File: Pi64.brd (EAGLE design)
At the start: 130.7 x 72.9 mm, 117 parts, among them J1 USB-MINIB-5PIN, J2 AVR_SPI, J3 FTDI_DEVICERA_SMT, J4 FTDI_DEVICERA_SMT, SW1 LEFT, SW2 RIGHT, SW3 PWR_SWITCH, SW8 OS102011MA1Q, U1 MIC7221, U2 MCP1642B-ADJ, U3 PAM2306AYPKE, U4 LM4875, U5 Mic5365-2.8Y, U7 AZV321, X2 HEADPHONE

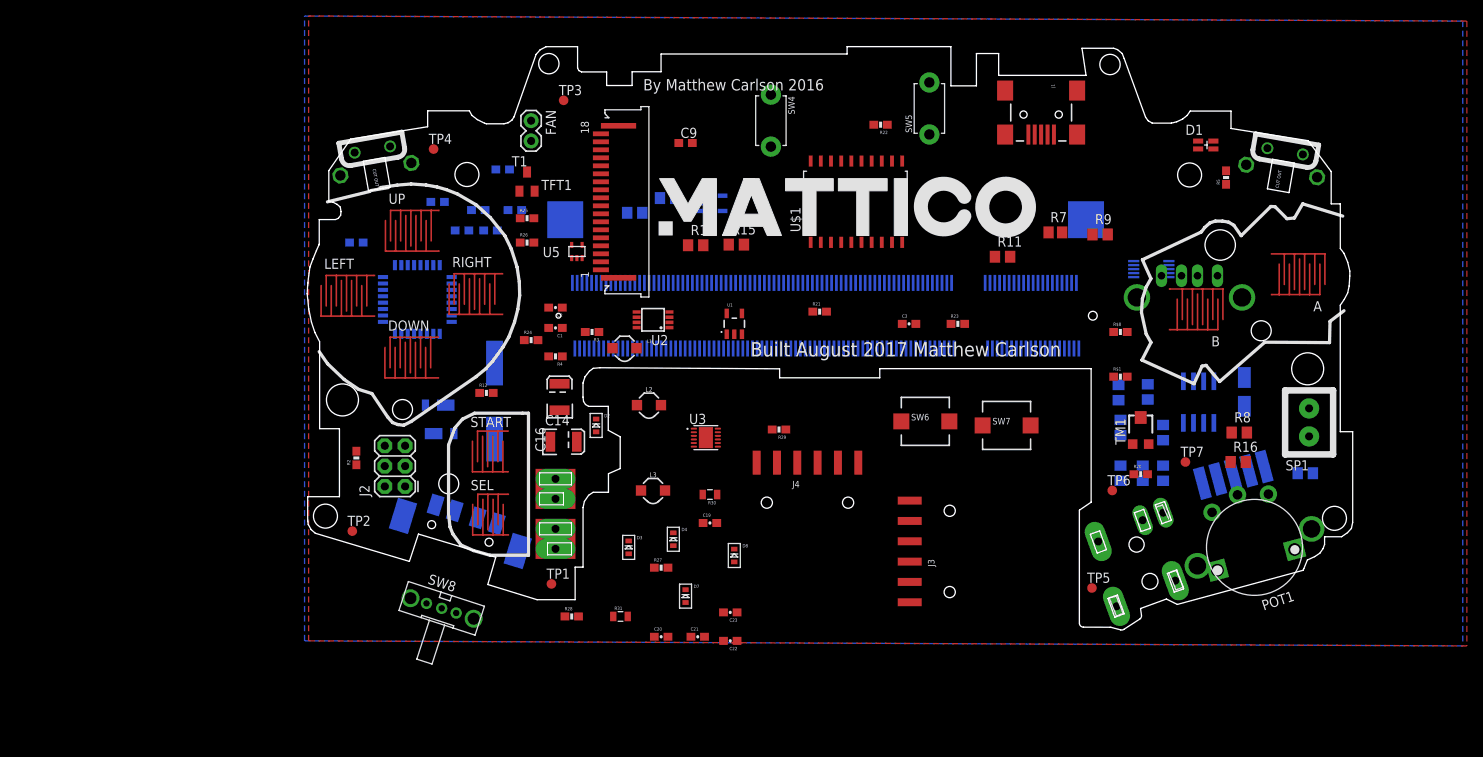
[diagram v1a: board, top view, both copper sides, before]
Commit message: Removed old stuff and started new circuit board design
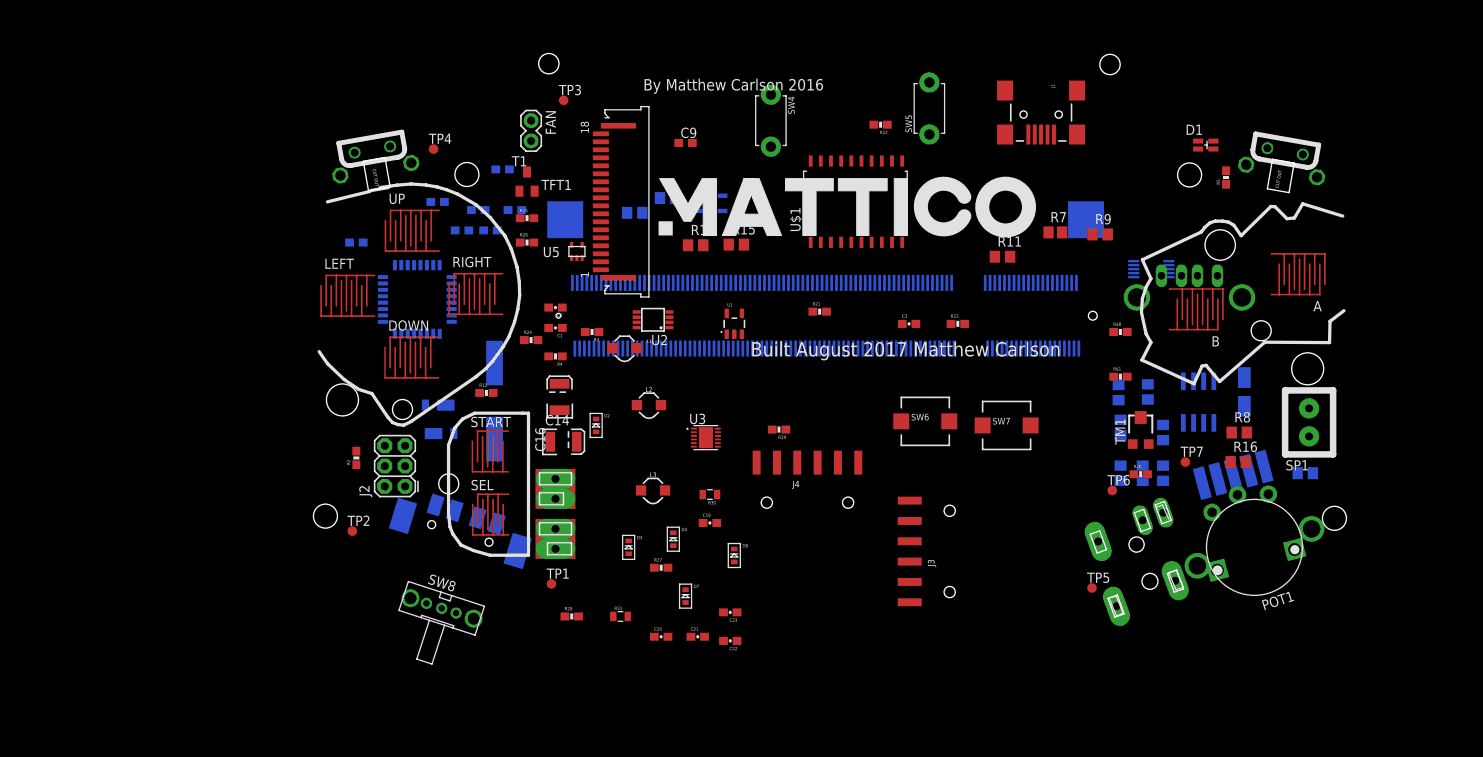
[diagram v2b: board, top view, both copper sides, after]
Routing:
- removed copper zone on layer 1, net GND
- removed copper zone on layer 16, net GND
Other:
- board size 130.7 x 72.9 mm -> 11.7 x 14.5 mm

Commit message: removed a lot of cruft and added STM32F
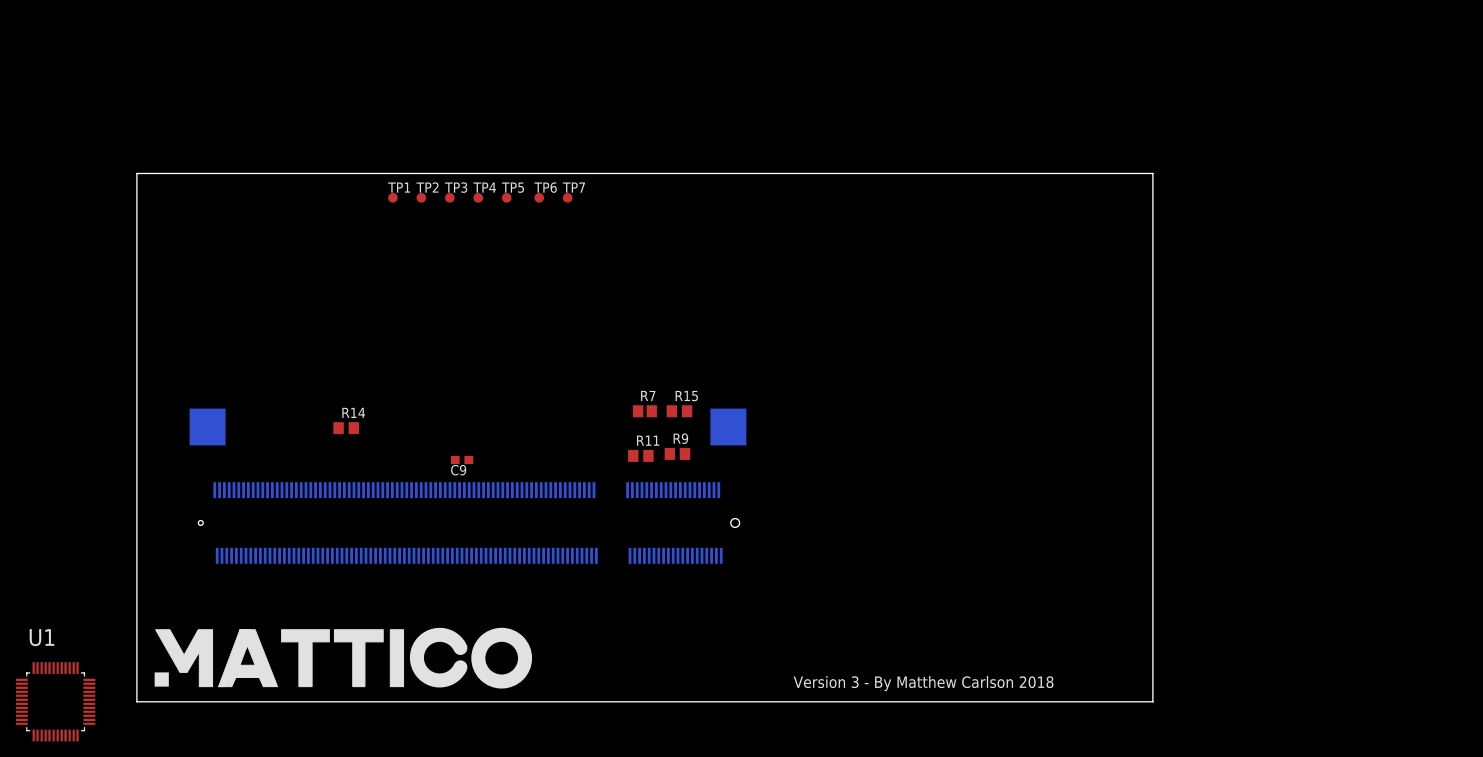
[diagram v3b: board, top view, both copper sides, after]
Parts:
- removed A, B, DOWN, LEFT, RIGHT, UP: GBA_BTN_CONDUCTIVE, GBA:GBA_BUTTON_CONDUCTIVE
- removed BT1: (no value), custom:GBA_BATTERY
- removed C1, C19, C2, C3: 100nF, SparkFun-Capacitors:0603-CAP
- removed C10: 1.0uF, SparkFun-Capacitors:0603-CAP
- removed C11, C12: 22pF, SparkFun-Capacitors:0603-CAP
- removed C13, C15, C18, C5, C6: 10u, rcl:C0805
- removed C14, C16: 47uF, SparkFun-Capacitors:EIA3528
- removed C17: 100n, rcl:C0805
- removed C20, C21, C22, C23: 10uF, SparkFun-Capacitors:0603-CAP
- removed C4: 220n, rcl:C0805
- removed C7: 100uF, rcl:153CLV-0405
- removed C8: 330n, rcl:C0805
- removed COPRO: MEGA16u2, adafruit:TQFP32-08
- removed D1: DUAL_LED, custom:DUAL_LED
- removed D2, D3, D4, D7, D8: (no value), adafruit:SOD-523
- removed D5, D6: (no value), custom:DIODE_POWERDI_123
- removed FAN: (no value), SparkFun-Connectors:1X02
- removed J1: USB-MINIB-5PIN, SparkFun-Connectors:USB-MINIB
- removed J2: AVR_SPI, SparkFun-Connectors:2X3
- removed J3, J4: FTDI_DEVICERA_SMT, SparkFun-Connectors:FTDI_DEVICE_RA_SMT
- removed L1: 4.7uH, SparkFun-Passives:INDUCTOR_4.7UH
- removed L2, L3: 4.7µH/±30%/1.2A, SparkFun-Coils:INDUCTOR_4.7UH
- removed POT1: THUMBPOT, adafruit:THUMBWHEEL
- removed R$1: 976kR, SparkFun-Resistors:0603-RES
- removed R$8: 430kR, SparkFun-Resistors:0603-RES
- removed R1: 27k, GBA:VOLUME
- removed R10: 3R9, rcl:R0805
- removed R12: 1K, SparkFun-Resistors:0603-RES
- removed R13, R2, R21, R22, R25, R26: 4.7K, SparkFun-Resistors:0603-RES
- removed R16, R8: 270R, rcl:R0805
- removed R17, R18: 22, SparkFun-Resistors:0603-RES
- removed R19, R24, R27, R28: 10K, SparkFun-Resistors:0603-RES
- removed R20, R5: 680, SparkFun-Resistors:0603-RES
- removed R23, R29, R3: 100k, SparkFun-Resistors:0603-RES
- removed R30, R31: (no value), SparkFun-Resistors:0805
- removed R4: 270, SparkFun-Resistors:0603-RES
- removed R6: 100k, rcl:R0805
- removed SEL, START: BUTTON-CONDUCTIVESMD, SparkFun-Electromechanical:BUTTON-CONDUCTIVE
- removed SP1: SPEAKER, GBA:SPEAKER
- removed SW1: LEFT, GBA:BUMPER
- removed SW2: RIGHT, GBA:BUMPER
- removed SW3: PWR_SWITCH, GBA:PWR_SWITCH
- removed SW4, SW5: (no value), adafruit:TACT_PANA-EVQ
- removed SW6, SW7: (no value), adafruit:PUSHBUTTON_SMD_SJ
- removed SW8: OS102011MA1Q, adafruit:OS102011MA1Q
- removed T1: (no value), custom:TRANSISTOR_SC59-BEC
- removed TFT1: GBA_TFT, GBA:GBA_TFT
- removed TM1: (no value), adafruit:TC33X
- removed U$1: CBT3244AD, custom:S020-75MM
- removed U$3: MCP48FEB01-E/UN, custom:10-MSOP
- removed U$5: CRYSTAL-ABLS, custom:HC49/US
- removed U2: MCP1642B-ADJ, custom:MICROCHIP_MSOP8
- removed U3: PAM2306AYPKE, custom:SON45P300X300X80-13N
- removed U4: LM4875, texas:SOIC8
- removed U5: Mic5365-2.8Y, SparkFun-PowerIC:SC70
- removed U7: AZV321, GBA:SOT23-5
- removed X1: (no value), Adafruit_PowerBoost:MICROBUILDER_USB_HOST-PTH
- removed X2: HEADPHONE, GBA:HEADPHONE
- U1: value MIC7221 -> STM32F103CBT6; device custom:SPARKFUN-ANALOGIC_SOT23-5 -> custom:QFP50P900X900X160-48N
- moved U1 97.1 mm to (-10.2, 0.00)
- moved TP5 87.9 mm to (46.2, 63.0)
- moved U$2 84.5 mm to (1.58, 1.14)
- moved TP7 84.0 mm to (53.8, 63.0)
- moved TP6 80.4 mm to (50.3, 63.0)
- moved R9 59.5 mm to (67.6, 31.0)
- moved R7 56.0 mm to (63.5, 36.3)
- moved TP1 52.2 mm to (32.0, 63.0)
- moved PCB1 51.7 mm to (41.7, 22.4)
- moved R11 51.6 mm to (63.0, 30.7)
- moved R14 49.3 mm to (26.2, 34.2)
- moved C9 48.5 mm to (40.6, 30.2), turned to 180 degrees
- moved TP2 42.5 mm to (35.6, 63.0)
- moved FRAME2 29.0 mm to (32.0, -9.65)
- moved R15 22.0 mm to (67.8, 36.3)
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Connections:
- removed net BATT_LOW: D1.1, D1.3, D8.A, R3.2, U1.1
- removed net COPRO_D+: R18.1
- removed net COPRO_D-: R17.1
- removed net COPRO_DC: COPRO.20, U$1.P$8
- removed net COPRO_MISO: COPRO.17, J2.1, U$3.8
- removed net COPRO_MOSI: COPRO.16, J2.4, U$1.P$4, U$3.10
- removed net COPRO_RESET: COPRO.24, J2.5, R19.1
- removed net COPRO_RX: COPRO.8
- removed net COPRO_SCK: COPRO.15, J2.3, U$1.P$2, U$3.9
- removed net COPRO_TFT_RESET: COPRO.14, U$1.P$6
- removed net COPRO_TX: COPRO.9
- removed net DAC_CS: COPRO.19, U$3.2
- removed net DAC_OUT: R16.1, U$3.4
- removed net DAC_REF: U$3.3
- removed net EXP: U3.13
- removed net FAN_EN: R12.2
- removed net N$10: R22.1, U$1.P$19
- removed net N$11: C5.1, U4.7
- removed net N$12: COPRO.5, R28.1
- removed net N$13: C7.-, X2.L, X2.R
- removed net N$14: C7.+, SP1.1, U4.5
- removed net N$15: SP1.2, U4.8
- removed net N$16: R6.1, U4.3, X2.2
- removed net N$18: R21.1, U$1.P$1
- removed net N$19: COPRO.30, R17.2
- removed net N$2: C4.1, C8.1, R16.2, R8.2
- removed net N$21: R10.2, TFT1.10
- removed net N$22: COPRO.29, R18.2
- removed net N$23: R$1.1, R$8.2, U2.2
- removed net N$24: R10.1, U7.3, U7.4
- removed net N$25: C10.1, COPRO.27
- removed net N$28: C11.1, COPRO.1, U$5.P$2
- removed net N$29: C12.1, COPRO.2, U$5.P$1
- removed net N$3: D7.A, D8.K
- removed net N$31: D3.A, D4.K
- removed net N$32: L3.P$1, U3.2
- removed net N$33: D3.K, D7.K, R27.2, R28.2
- removed net N$34: L1.P$2, U2.5
- removed net N$38: COPRO.22, R27.1
- removed net N$39: FAN.1, T1.C
- removed net N$4: C2.1, R3.1, TM1.2, U1.3
- removed net N$40: R12.1, T1.B
- removed net N$44: COPRO.6, R24.1
- removed net N$45: C14.A, D5.2, D6.2, L1.P$1, SW8.2, U2.8
- removed net N$46: C19.1, R29.1, U3.12
- removed net N$47: L2.P$1, U3.8
- removed net N$49: R31.2, U3.4
- removed net N$5: C1.1, R4.1, U1.4
- removed net N$50: R30.1, U3.10
- removed net N$6: D1.4, R5.1
- removed net N$7: D1.2, R20.2
- removed net N$8: POT1.2, U4.4
- removed net N$9: C4.2, U4.2
- removed net PWR_DOWN: D2.A, D4.A, SW8.1
- removed net PWR_UP: D2.K, R23.2, R24.2, U2.1
- removed net TFT_CS: COPRO.10, TFT1.5
- removed net TFT_DC: TFT1.4, U$1.P$12, U$1.P$3
- removed net TFT_MOSI: TFT1.6, U$1.P$16, U$1.P$7
- removed net TFT_RESET: TFT1.2, U$1.P$14, U$1.P$5
- removed net TFT_SCLK: TFT1.3, U$1.P$18, U$1.P$9
- removed net USB_GND: J1.GND
- removed net V_BATT: BT1.BT+1, BT1.BT+2, D6.1, R4.2
- removed net V_USB: D5.1, J1.VBUS
- new net +3V3: U1.1, U1.24, U1.36, U1.48, U1.9
- new net PA11: U1.32
- net 1.8V: no longer C20.1, L3.P$2, R30.2
- net 2.8V: no longer C13.1, TFT1.9, U5.5
- net 3.3V: no longer C21.1, COPRO.31, COPRO.32, COPRO.4, L2.P$2, R13.2, R2.2, R21.2, R22.2, R25.2, R26.2, R31.1, U$1.P$20, U$3.1
- net 5V: no longer C15.1, C16.A, C17.1, C18.1, C22.1, C23.1, C3.1, C6.2, FAN.2, J2.2, POT1.3, R$1.2, R19.2, R29.2, R5.2, R6.2, TM1.3, U1.2, U2.4, U3.1, U3.6, U3.7, U4.1, U5.1, U5.3, U7.5, X1.VBUS
- net A_BTN: no longer A.2
- net B_BTN: no longer B.2
- net DOWN_BTN: no longer DOWN.2
- net GND: no longer A.1, B.1, BT1.BT-1, BT1.BT-2, C1.2, C10.2, C11.2, C12.2, C13.2, C14.C, C15.2, C16.C, C17.2, C18.2, C19.2, C2.2, C20.2, C21.2, C22.2, C23.2, C3.2, C5.2, C6.1, C8.2, COPRO.28, COPRO.3, DOWN.1, J2.6, J3.6, J4.6, LEFT.1, POT1.1, R$8.1, R20.1, R23.1, RIGHT.1, SEL.1, START.1, SW1.1, SW2.1, SW4.P$2, SW5.P$2, SW6.P$2, SW7.P$2, T1.E, TFT1.1, TFT1.11, TFT1.12, TFT1.13, TFT1.14, TFT1.8, TM1.1, U$1.P$10, U$3.7, U1.5, U2.6, U2.7, U3.3, U3.9, U4.6, U5.2, U7.2, UP.1, X1.GND, X2.1, X2.GND
- net L1_BTN: no longer SW1.2
- net L2_BTN: no longer R2.1, SW4.P$1
- net LEFT_BTN: no longer LEFT.2
- net PI_MOSI: no longer U$1.P$13
- net PI_PWM0: no longer R8.1
- net PI_SCK: no longer U$1.P$11
- net PI_TFT_DC: no longer U$1.P$17
- net PI_TFT_RESET: no longer U$1.P$15
- net R1_BTN: no longer SW2.2
- net R2_BTN: no longer R13.1, SW5.P$1
- net RIGHT_BTN: no longer RIGHT.2
- net SELECT_BTN: no longer SEL.2
- net START_BTN: no longer START.2
- net TFT_LED: no longer U7.1
- net UP_BTN: no longer UP.2
- net X_BTN: no longer R26.1, SW6.P$1
- net Y_BTN: no longer R25.1, SW7.P$1
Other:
- board size 11.7 x 14.5 mm -> 127 x 66 mm
- board text added: "Designed October 2018 Matthew Carlson"
- board text added: "Version 3 - By Matthew Carlson 2018"
- board text removed: "Built August 2017 Matthew Carlson"
- board text removed: "By Matthew Carlson 2016"

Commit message: Added PWR and GND to STM32
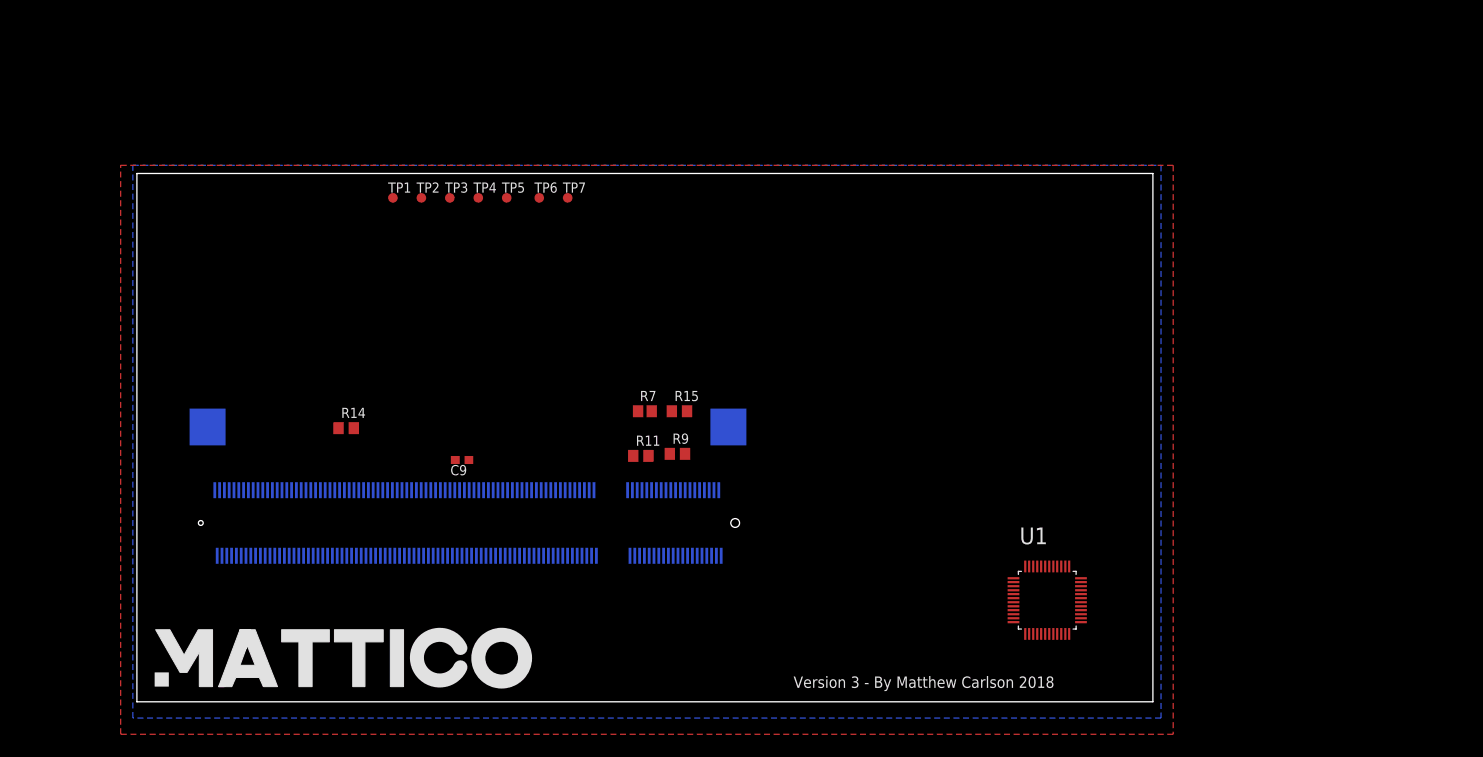
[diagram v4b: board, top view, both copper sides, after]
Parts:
- moved U1 124.6 mm to (113.8, 12.7)
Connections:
- net GND: now also U1.23, U1.35, U1.44, U1.47, U1.8
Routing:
- added copper zone on layer 1, net GND
- added copper zone on layer 16, net GND
